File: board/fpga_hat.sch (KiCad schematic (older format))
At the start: 29 parts

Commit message: Probably time for another commit :)
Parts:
- added C? (x2): 10u, symbol Device:C_Small
- added R? (x2): 100, symbol Device:R_Small
- added U?: IS61WV25616, symbol fpga_hat:IS61WV25616
- added U? (x6): iCE40-HX8k-BG121, symbol fpga_hat:iCE40-HX8k-BG121
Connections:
- net +3V3: now also U?.C10 (VPP_2V5), U?.D6 (VCCIO_0), U?.E4 (VCCIO_3), U?.F8 (VCCIO_1), U?.G4 (VCCIO_3), U?.H6 (VCCIO_2), U?.L11 (VCC_SPI)
- net GND: now also U?.E5 (GND), U?.E6 (GND), U?.E7 (GND), U?.F5 (GND), U?.F6 (GND), U?.F7 (GND), U?.G5 (GND), U?.G6 (GND), U?.G7 (GND), U?.H5 (GND)
- net GP10_SPI_MOSI: now also U?.K9 (IOB_105_SDO)
- net GP11_SPI_SCK: now also U?.L10 (IOB_107_SCK)
- net GP12_FPGA_~RST: now also U?.L9 (CRESET_B)
- net GP13_FPGA_CDONE: now also U?.K8 (CDONE)
- net GP8_SPI_~CS: now also U?.K10 (IOB_108_SS)
- net GP9_SPI_MISO: now also U?.J9 (IOB_106_SDI)
- new net: C?.2, U?.C5 (GNDPLL1)
- new net: C?.1, R?.1, U?.C6 (VCCPLL1)
- new net: C?.1, R?.1, U?.J6 (VCCPLL0)
- new net: C?.2, U?.L6 (GNDPLL0)
- new net +1V2: R?.2, R?.2, U?.D4 (VCC), U?.D8 (VCC), U?.H4 (VCC), U?.H8 (VCC)
- no-connect marks 0 -> 1
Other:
- note added: "512 kB (256k x 16b) Async SRAM"
- note added: "Note:\n- VPP_2V5 can be tied to 3V3 when not using NVCM\n- VPP_FAST should be floating when not programming NVCM\n- PLL GNDs are tied inside FPGA, and should *not* be tied\n to board GND. Just exposed for bypass of PLL supply."

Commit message: Add SRAM BGA footprint, and add it to schematic
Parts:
- added C?: 100n, symbol Device:C
- added U?: DSC60XX, symbol fpga_hat:DSC60XX
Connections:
- net +3V3: now also U?.D6 (VDD), U?.E1 (VDD), C?.1, U?.1 (STBY), U?.4 (VCC)
- net GND: now also U?.B5 (~CE), U?.D1 (VSS), U?.E6 (VSS), C?.2, U?.2 (GND)
- net SRAM_~LB: now reaches U?.A1 (~LB)
- net SRAM_~LB: now also U?.H7 (IOB_87)
- net SRAM_~OE: now reaches U?.A2 (~OE)
- net SRAM_~OE: now also U?.K5 (IOB_79)
- net SRAM_A0: now reaches U?.A3 (A0)
- net SRAM_A0: now also U?.G3 (IOLB_17A)
- net SRAM_A1: now reaches U?.A4 (A1)
- net SRAM_A1: now also U?.H3 (IOL_17B)
- net SRAM_A2: now reaches U?.A5 (A2)
- net SRAM_A2: now also U?.H1 (IOL_18A)
- net SRAM_DQ8: now reaches U?.B1 (DQ8)
- net SRAM_DQ8: now also U?.D2 (IOL_9A)
- net SRAM_~UB: now reaches U?.B2 (~UB)
- net SRAM_~UB: now also U?.J7 (IOB_86)
- net SRAM_A3: now reaches U?.B3 (A3)
- net SRAM_A3: now also U?.H2 (IOL_18B)
- net SRAM_A4: now reaches U?.B4 (A4)
- net SRAM_A4: now also U?.J1 (IOL_23A)
- net SRAM_DQ0: now reaches U?.B6 (DQ0)
- net SRAM_DQ0: now also U?.B1 (IOL_2A)
- net SRAM_DQ9: now reaches U?.C1 (DQ9)
- net SRAM_DQ9: now also U?.D3 (IOL_9B)
- net SRAM_DQ10: now reaches U?.C2 (DQ10)
- net SRAM_DQ10: now also U?.E2 (IOL_10A)
- net SRAM_A5: now reaches U?.C3 (A5)
- net SRAM_A5: now also U?.K1 (IOL_23B)
- net SRAM_A6: now reaches U?.C4 (A6)
- net SRAM_A6: now also U?.K2 (IOL_25A)
- net SRAM_DQ1: now reaches U?.C5 (DQ1)
- net SRAM_DQ1: now also U?.B2 (IOL_2B)
- net SRAM_DQ2: now reaches U?.C6 (DQ2)
- net SRAM_DQ2: now also U?.C4 (IOL_4A)
- net SRAM_DQ11: now reaches U?.D2 (DQ11)
- net SRAM_DQ11: now also U?.E3 (IOL_10B)
- net SRAM_A17: now reaches U?.D3 (A17)
- net SRAM_A17: now also U?.K4 (IOB_73)
- net SRAM_A7: now reaches U?.D4 (A7)
- net SRAM_A7: now also U?.J2 (IOL_25B)
- net SRAM_DQ3: now reaches U?.D5 (DQ3)
- net SRAM_DQ3: now also U?.C3 (IOL_4B)
- net SRAM_DQ12: now reaches U?.E2 (DQ12)
- net SRAM_DQ12: now also U?.F1 (IOL_12A)
- net SRAM_A16: now reaches U?.E4 (A16)
- net SRAM_A16: now also U?.L4 (IOB_72)
- net SRAM_DQ4: now reaches U?.E5 (DQ4)
- net SRAM_DQ4: now also U?.C2 (IOL_5A)
- net SRAM_DQ14: now reaches U?.F1 (DQ14)
- net SRAM_DQ14: now also U?.F4 (IOL_13A)
- net SRAM_DQ13: now reaches U?.F2 (DQ13)
- net SRAM_DQ13: now also U?.F2 (IOL_12B)
- net SRAM_A14: now reaches U?.F3 (A14)
- net SRAM_A14: now also U?.J4 (IOB_64)
- net SRAM_A15: now reaches U?.F4 (A15)
- net SRAM_A15: now also U?.L3 (IOB_71)
- net SRAM_DQ5: now reaches U?.F5 (DQ5)
- net SRAM_DQ5: now also U?.C1 (IOL_5B)
- net SRAM_DQ6: now reaches U?.F6 (DQ6)
- net SRAM_DQ6: now also U?.E1 (IOL_8A)
- net SRAM_DQ15: now reaches U?.G1 (DQ15)
- net SRAM_DQ15: now also U?.G2 (IOL_14B)
- net SRAM_A12: now reaches U?.G3 (A12)
- net SRAM_A12: now also U?.L2 (IOB_61)
- net SRAM_A13: now reaches U?.G4 (A13)
- net SRAM_A13: now also U?.K3 (IOB_63)
- net SRAM_~WE: now reaches U?.G5 (~WE)
- net SRAM_~WE: now also U?.J5 (IOB_78)
- net SRAM_DQ7: now reaches U?.G6 (DQ7)
- net SRAM_DQ7: now also U?.D1 (IOL_8B)
- net SRAM_A8: now reaches U?.H2 (A8)
- net SRAM_A8: now also U?.F3 (IOL_13B_GBIN7)
- net SRAM_A9: now reaches U?.H3 (A9)
- net SRAM_A9: now also U?.G1 (IOL_14A_GBIN6)
- net SRAM_A10: now reaches U?.H4 (A10)
- net SRAM_A10: now also U?.L1 (IOB_56)
- net SRAM_A11: now reaches U?.H5 (A11)
- net SRAM_A11: now also U?.J3 (IOB_57)
- net IO0_0N renamed IO0_4
- net IO0_0P renamed IO0_0
- net IO0_1N renamed IO0_5
- net IO0_1P renamed IO0_1
- net IO0_2N renamed IO0_6
- net IO0_2P renamed IO0_2
- net IO0_3N renamed IO0_7
- net IO0_3P renamed IO0_3
- net IO1_0N renamed IO1_4
- net IO1_0P renamed IO1_0
- net IO1_1N renamed IO1_5
- net IO1_1P renamed IO1_1
- net IO1_2N renamed IO1_6
- net IO1_2P renamed IO1_2
- net IO1_3N renamed IO1_7
- net IO1_3P renamed IO1_3
- net IO2_0N renamed IO2_4
- net IO2_0P renamed IO2_0
- net IO2_1N renamed IO2_5
- net IO2_1P renamed IO2_1
- net IO2_2N renamed IO2_6
- net IO2_2P renamed IO2_2
- net IO2_3N renamed IO2_7
- net IO2_3P renamed IO2_3
- new net CLK_OSC: U?.3 (OUT)
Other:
- note added: "12 MHz MEMS oscillator\n"
- note added: "iCE40 FPGA\n"
- note removed: "Each pair of pins on this header is a differential pair\nrouted differentially from the iCE40. For low speed they\ncan still be used single-ended."
- moved on the sheet: C?, J?, R?, U?, U?A, U?B, U?C, U?D, U?E, U?F

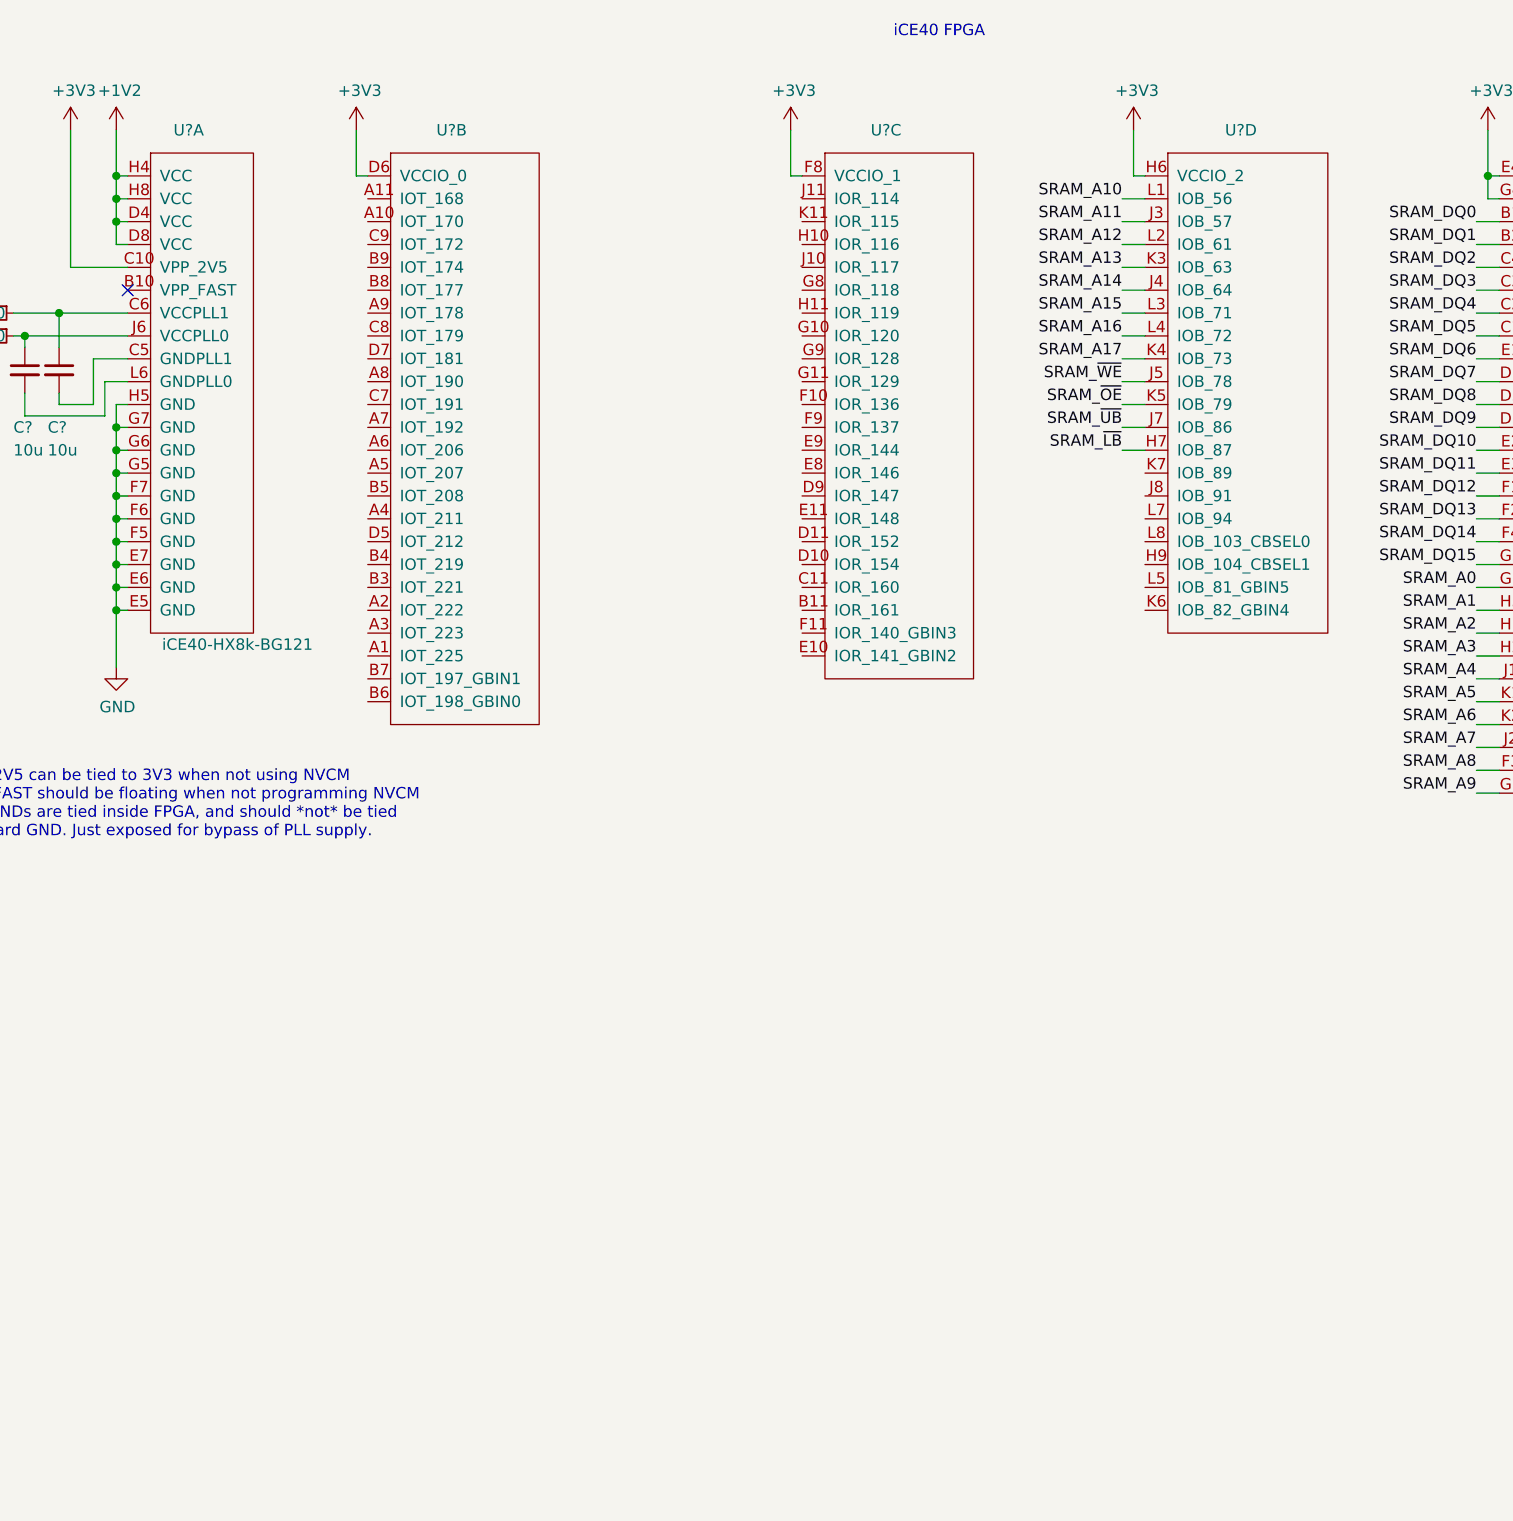
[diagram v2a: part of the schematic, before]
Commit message: Add switches and LEDs
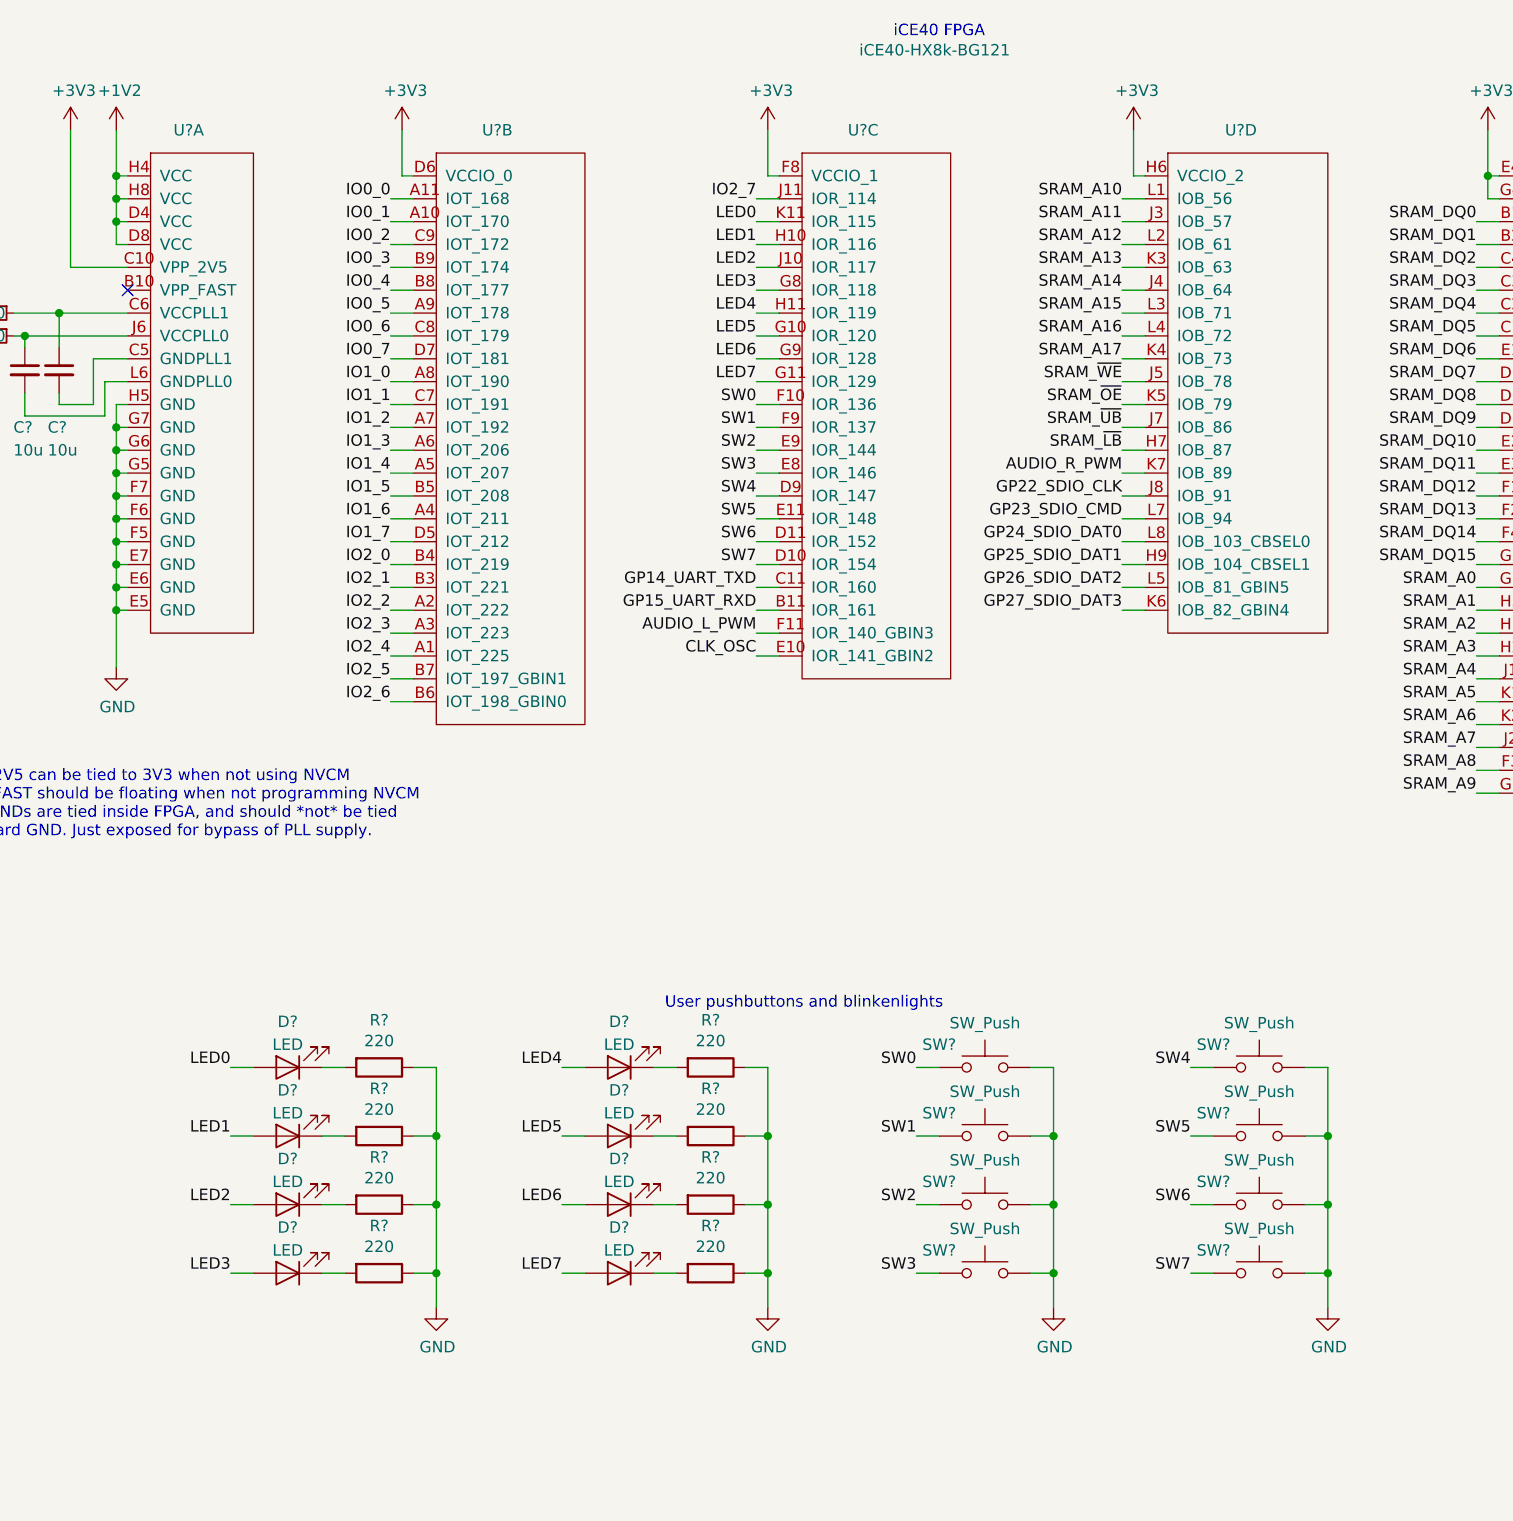
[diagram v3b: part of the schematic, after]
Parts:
- added D? (x8): LED, symbol Device:LED
- added R? (x8): 220, symbol Device:R
- added SW? (x8): SW_Push, symbol Switch:SW_Push
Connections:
- net AUDIO_L_PWM: now also U?.F11 (IOR_140_GBIN3)
- net AUDIO_R_PWM: now also U?.K7 (IOB_89)
- net CLK_OSC: now also U?.E10 (IOR_141_GBIN2)
- net GND: now also R?.1, R?.1, R?.1, R?.1, R?.1, R?.1, R?.1, R?.1, SW?.2, SW?.2, SW?.2, SW?.2, SW?.2, SW?.2, SW?.2, SW?.2
- net GP14_UART_TXD: now also U?.C11 (IOR_160)
- net GP15_UART_RXD: now also U?.B11 (IOR_161)
- net GP22_SDIO_CLK: now also U?.J8 (IOB_91)
- net GP23_SDIO_CMD: now also U?.L7 (IOB_94)
- net GP24_SDIO_DAT0: now also U?.L8 (IOB_103_CBSEL0)
- net GP25_SDIO_DAT1: now also U?.H9 (IOB_104_CBSEL1)
- net GP26_SDIO_DAT2: now also U?.L5 (IOB_81_GBIN5)
- net GP27_SDIO_DAT3: now also U?.K6 (IOB_82_GBIN4)
- net IO0_0: now also U?.A11 (IOT_168)
- net IO0_1: now also U?.A10 (IOT_170)
- net IO0_2: now also U?.C9 (IOT_172)
- net IO0_3: now also U?.B9 (IOT_174)
- net IO0_4: now also U?.B8 (IOT_177)
- net IO0_5: now also U?.A9 (IOT_178)
- net IO0_6: now also U?.C8 (IOT_179)
- net IO0_7: now also U?.D7 (IOT_181)
- net IO1_0: now also U?.A8 (IOT_190)
- net IO1_1: now also U?.C7 (IOT_191)
- net IO1_2: now also U?.A7 (IOT_192)
- net IO1_3: now also U?.A6 (IOT_206)
- net IO1_4: now also U?.A5 (IOT_207)
- net IO1_5: now also U?.B5 (IOT_208)
- net IO1_6: now also U?.A4 (IOT_211)
- net IO1_7: now also U?.D5 (IOT_212)
- net IO2_0: now also U?.B4 (IOT_219)
- net IO2_1: now also U?.B3 (IOT_221)
- net IO2_2: now also U?.A2 (IOT_222)
- net IO2_3: now also U?.A3 (IOT_223)
- net IO2_4: now also U?.A1 (IOT_225)
- net IO2_5: now also U?.B7 (IOT_197_GBIN1)
- net IO2_6: now also U?.B6 (IOT_198_GBIN0)
- net IO2_7: now also U?.J11 (IOR_114)
- net SW7: now reaches U?.D10 (IOR_154)
- net SW7: now also SW?.1
- net SW6: now reaches U?.D11 (IOR_152)
- net SW6: now also SW?.1
- net SW4: now reaches U?.D9 (IOR_147)
- net SW4: now also SW?.1
- net SW5: now reaches U?.E11 (IOR_148)
- net SW5: now also SW?.1
- net SW3: now reaches U?.E8 (IOR_146)
- net SW3: now also SW?.1
- net SW2: now reaches U?.E9 (IOR_144)
- net SW2: now also SW?.1
- net SW0: now reaches U?.F10 (IOR_136)
- net SW0: now also SW?.1
- net SW1: now reaches U?.F9 (IOR_137)
- net SW1: now also SW?.1
- net LED5: now reaches U?.G10 (IOR_120)
- net LED5: now also D?.2 (A)
- net LED7: now reaches U?.G11 (IOR_129)
- net LED7: now also D?.2 (A)
- net LED3: now reaches U?.G8 (IOR_118)
- net LED3: now also D?.2 (A)
- net LED6: now reaches U?.G9 (IOR_128)
- net LED6: now also D?.2 (A)
- net LED1: now reaches U?.H10 (IOR_116)
- net LED1: now also D?.2 (A)
- net LED4: now reaches U?.H11 (IOR_119)
- net LED4: now also D?.2 (A)
- net LED2: now reaches U?.J10 (IOR_117)
- net LED2: now also D?.2 (A)
- net LED0: now reaches U?.K11 (IOR_115)
- net LED0: now also D?.2 (A)
- new net: D?.1 (K), R?.2 (x8)
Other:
- note added: "User pushbuttons and blinkenlights\n"
- moved on the sheet: U?B, U?C

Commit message: Add datasheet for SRAM, core regulator. Add core regulator to schematic. Some tidy-up.
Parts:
- added C?: 560p, symbol Device:C
- added C? (x2): 4u7, symbol Device:C
- added L?: L, symbol Device:L
- added U?: MIC23050, symbol fpga_hat:MIC23050
- C? (x4): value 10u -> 4u7
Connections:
- net +1V2: now also C?.1, C?.1, L?.2, U?.4 (SNS)
- net +5V: now also C?.1, U?.2 (EN), U?.7 (VIN)
- net GND: now also C?.2, C?.2, U?.6 (AGND), U?.8 (PGND)
- new net: L?.1, U?.1 (SW)
- new net: C?.2, U?.5 (CFF)
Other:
- note added: "Audio LDO\n(The Pi's 3V3 is used instead for VDDIO,\nand downstream PMOD power.)"
- note added: "Core power supply for FPGA\n"
- note added: "This is just the reference circuit.\nReference layout shows AGND tied to the under-pad ONLY,\nand PGND tied to bypass, board GND and the under-pad."
- moved on the sheet: C?, D?, J?, R?, SW?, U?, U?A, U?B, U?C

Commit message: Add more datasheets. Add FPGA decoupling. Add button + LED for FPGA RST/CDONE
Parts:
- removed R? (x4): 220, symbol Device:R
- added C? (x8): 100n, symbol Device:C
- added D?: LED, symbol Device:LED
- added R?: 4k7, symbol Device:R
- added R? (x5): 470, symbol Device:R
- added SW?: SW_Push, symbol Switch:SW_Push
- R? (x2): value 3k9 -> 4k7
- R? (x4): value 220 -> 470
- U?: value MIC23050 -> MIC23050-4YML
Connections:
- net +1V2: now also C?.1, C?.1, C?.1, C?.1
- net +3V3: now also C?.1, C?.1, C?.1, C?.1, R?.1
- net GND: now also C?.2, C?.2, C?.2, C?.2, C?.2, C?.2, C?.2, C?.2, D?.1 (K), R?.1, R?.1, R?.1, R?.1, SW?.2
- net GP12_FPGA_~RST: now also R?.2, SW?.1
- net GP13_FPGA_CDONE: now also D?.2 (A), R?.1
- net at D?.1 (K): now also R?.2 (x4)
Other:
- note added: "12 MHz MEMS oscillator\nPrimary FPGA clock input"
- note added: "Button + LED for FPGA reset + configuration (RED LED)\n\n"
- note added: "Core + VDDIO bypass for FPGA\n"
- note added: "User pushbuttons and blinkenlights (GREEN LEDs)"
- note removed: "12 MHz MEMS oscillator\n"
- note removed: "User pushbuttons and blinkenlights\n"
- moved on the sheet: C?, L?, R?, U?, U?A, U?B, U?C, U?D, U?E, U?F

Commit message: Add config flash, fix some ERC errors
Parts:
- removed R?: 1k, symbol Device:R
- added C17: 100n, symbol Device:C
- added R3: 470, symbol Device:R
- added U7: W25X40CL, symbol fpga_hat:W25X40CL
- gave numbers to parts that had none: 75
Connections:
- net +3V3: now also R18.2, C17.1, R3.1, U7.3 (~WP), U7.7 (~HOLD), U7.8 (VCC)
- net GND: now also C17.2, U7.4 (GND)
- net GP10_SPI_MOSI: now also U7.5 (MOSI/IO0)
- net GP11_SPI_SCK: now also U7.6 (SCK)
- net GP8_SPI_~CS: now also U7.1 (~CS)
- net GP9_SPI_MISO: now also U7.2 (MISO/IO1)
- net at JP1.1 (A), TP1.1, U2.7 (WP): now also R3.2
- no-connect marks 1 -> 13
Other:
- note added: "Config flash for FPGA\n4Mbit with dual I/O"
- note added: "Recommended circuit taken from\nhttps://github.com/raspberrypi/hats\nResistor values tweaked to reduce uniques"
- note removed: "Recommended circuit taken from\nhttps://github.com/raspberrypi/hats"
- moved on the sheet: C1, C11, C12, C13, C14, C15, C16, C22, C3, C5, C6, C7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
